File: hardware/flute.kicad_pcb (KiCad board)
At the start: 2 copper layers, 230 x 20 mm, 55 parts, among them J1 Conn_01x02, J3 Conn_01x04, SW1 C, SW2 D, SW3 E, SW4 F, SW5 G, SW6 A, SW7 H, SW8 OCTAVE?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

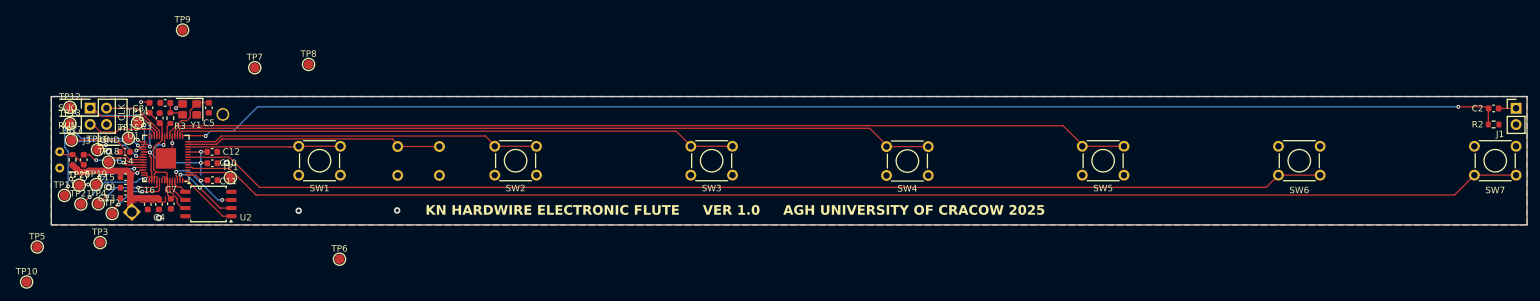
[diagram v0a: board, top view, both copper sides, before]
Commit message: test points placed on the pcb
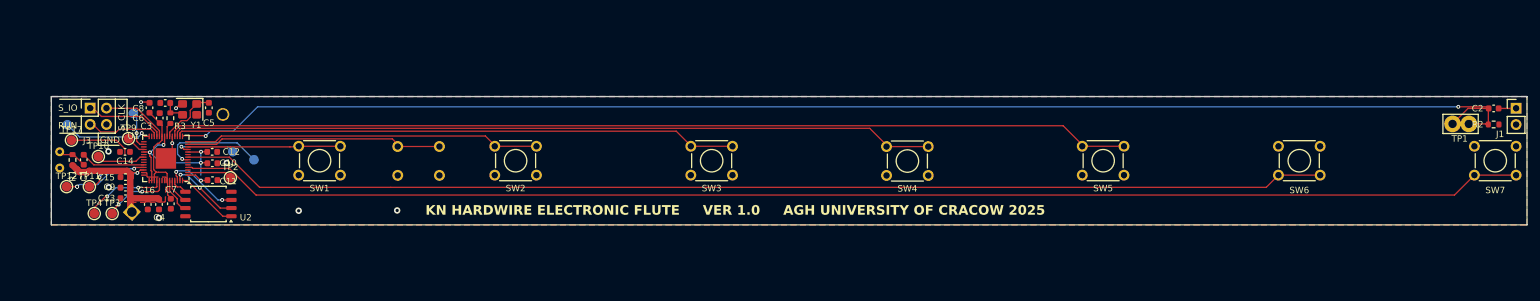
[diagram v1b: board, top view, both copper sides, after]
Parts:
- removed the TP11 at (35.7, 116.8)
- removed TP13, TP15, TP18, TP21: TestPoint, TestPoint:TestPoint_Pad_D1.5mm
- removed the TP3 at (41.3, 124.2)
- removed the TP5 at (31.5, 124.8)
- removed the TP7 at (65.4, 96.9)
- removed the TP9 at (54.2, 91.0)
- added TP1: TestPoint, TestPoint:TestPoint_Bridge_Pitch2.54mm_Drill1.3mm, F.Cu at (252.1, 105.7)
- TP5: renamed from TP6; moved to B.Cu
- TP6: renamed from TP8; moved to B.Cu
- TP7: renamed from TP10; moved to B.Cu
- TP8: renamed from TP12; moved to B.Cu
- moved TP7 25.3 mm to (36.2, 105.8)
- moved TP5 20.4 mm to (65.3, 111.3)
- moved TP6 18.0 mm to (62.0, 110.0)
- moved TP8 9.95 mm to (46.5, 104.0)
- moved TP9 2.87 mm to (45.7, 108.0)
- moved TP12 1.99 mm to (36.1, 115.4)
- moved TP4 1.65 mm to (40.4, 119.6)
- moved TP11 1.12 mm to (39.6, 115.4)
- moved TP10 1.07 mm to (41.0, 110.7)
- renumbered TP16 to TP10, TP19 to TP11, TP20 to TP12, TP1 to TP2, TP2 to TP3, TP14 to TP9
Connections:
- TP2 pad 2: Net-(U1-GPIO0) -> (no net)
- U1 pad 27: Net-(U1-GPIO16) -> /RASPBERRY_PI_PICO/GPIO16
- U1 pad 29: Net-(U1-GPIO18) -> /RASPBERRY_PI_PICO/GPIO18
- U1 pad 31: Net-(U1-GPIO20) -> /RASPBERRY_PI_PICO/GPIO20
- U1 pad 34: Net-(U1-GPIO22) -> /RASPBERRY_PI_PICO/GPIO22
- U1 pad 36: Net-(U1-GPIO24) -> /RASPBERRY_PI_PICO/GPIO24
- U1 pad 37: Net-(U1-GPIO25) -> /RASPBERRY_PI_PICO/GPIO25
- U1 pad 41: Net-(U1-GPIO29_ADC3) -> /RASPBERRY_PI_PICO/GPIO29
- U1 pad 5: Net-(U1-GPIO3) -> /RASPBERRY_PI_PICO/GPIO3
- U1 pad 6: Net-(U1-GPIO4) -> /RASPBERRY_PI_PICO/GPIO4
- U1 pad 9: Net-(U1-GPIO7) -> /RASPBERRY_PI_PICO/GPIO7
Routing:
- net Net-(U1-GPIO18): track 24.0 -> 0.00 mm, vias 2 -> 0
- net Net-(U1-GPIO5): track 0.00 -> 16.5 mm, vias 0 -> 1
- net Net-(U1-GPIO17): track 0.00 -> 14.0 mm, vias 0 -> 1
- net Net-(U1-GPIO20): track 14.0 -> 0.00 mm, vias 2 -> 0
- net Net-(U1-GPIO19): track 18.1 -> 5.86 mm, vias 2 -> 1
- net Net-(U1-GPIO29_ADC3): track 11.7 -> 0.00 mm, vias 2 -> 0
- net /PWM_OUT: track 208.2 -> 217.9 mm
- net Net-(U1-GPIO8): track 0.00 -> 9.50 mm, vias 0 -> 1
- net Net-(U1-GPIO25): track 6.05 -> 0.00 mm
- net Net-(U1-GPIO21): track 7.15 -> 3.09 mm, vias 2 -> 0
- net Net-(U1-GPIO24): track 13.1 -> 9.83 mm
- net Net-(U1-GPIO28_ADC2): track 11.0 -> 13.2 mm, vias 2 -> 3
- net /RASPBERRY_PI_PICO/USB_DM: track 11.2 -> 13.0 mm
- net Net-(U1-GPIO27_ADC1): track 8.89 -> 9.99 mm
- net Net-(U1-GPIO22): track 1.06 -> 0.00 mm
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
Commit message: minor corrections
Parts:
- removed TP1: TestPoint, TestPoint:TestPoint_Bridge_Pitch2.54mm_Drill1.3mm
- removed TP17: TestPoint, TestPoint:TestPoint_Pad_D1.5mm
- added JP1: COUPLING, Jumper:SolderJumper-2_P1.3mm_Open_Pad1.0x1.5mm, F.Cu at (252.7, 105.4)
- added JP2: NO_COUPLING, Jumper:SolderJumper-2_P1.3mm_Open_Pad1.0x1.5mm, F.Cu at (255.5, 105.4)
- moved TP5 0.52 mm to (64.8, 111.1)
- moved TP8 0.28 mm to (46.7, 104.1)
- moved TP6 0.13 mm to (62.0, 110.1)
- moved C15 0.10 mm to (45.2, 114.0)
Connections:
- C2 pad 2: /PWM_OUT -> Net-(JP1-A)
- R2 pad 1: /PWM_OUT -> Net-(JP1-A)
- TP2 pad 2: (no net) -> Net-(U1-GPIO0)
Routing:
- net Net-(U1-GPIO24): track 9.83 -> 0.00 mm
- net Net-(JP1-A): track 0.00 -> 7.74 mm
- net Net-(J1-Pin_1): track 2.74 -> 9.25 mm
- net /PWM_OUT: track 217.9 -> 213.6 mm

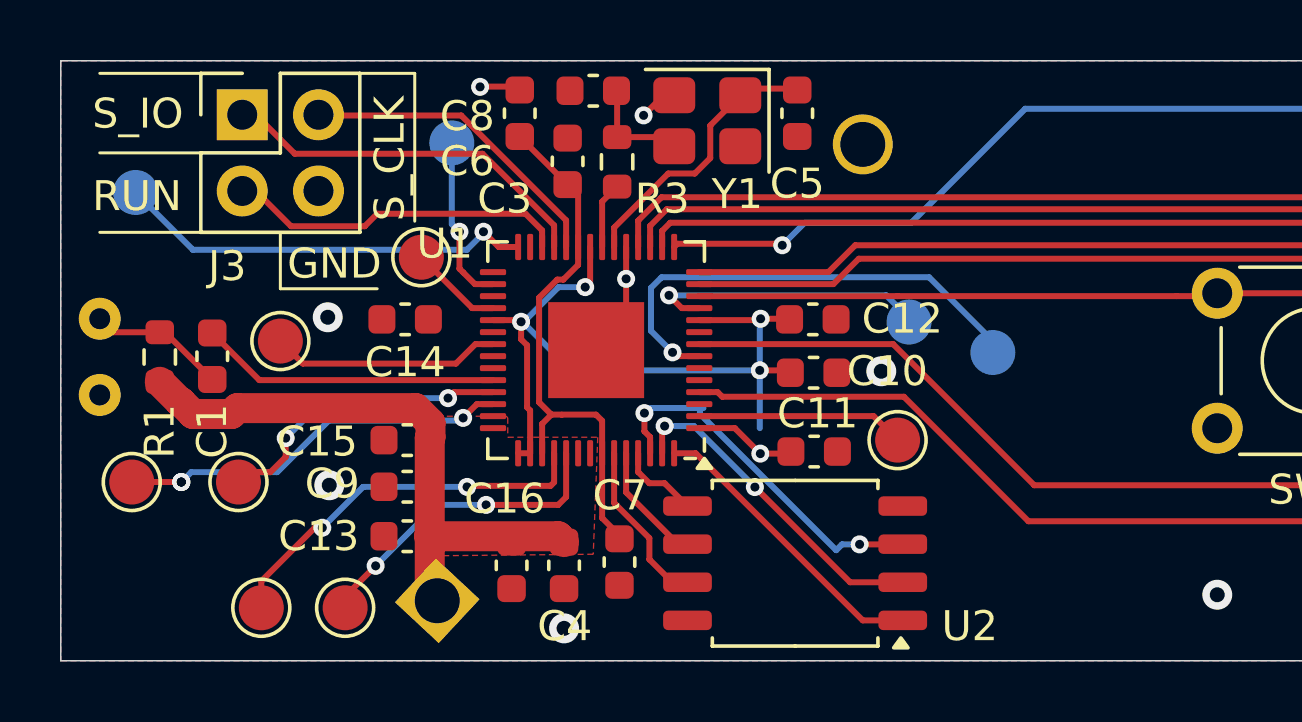
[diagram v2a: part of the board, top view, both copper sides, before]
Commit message: errors with elements placement corrected
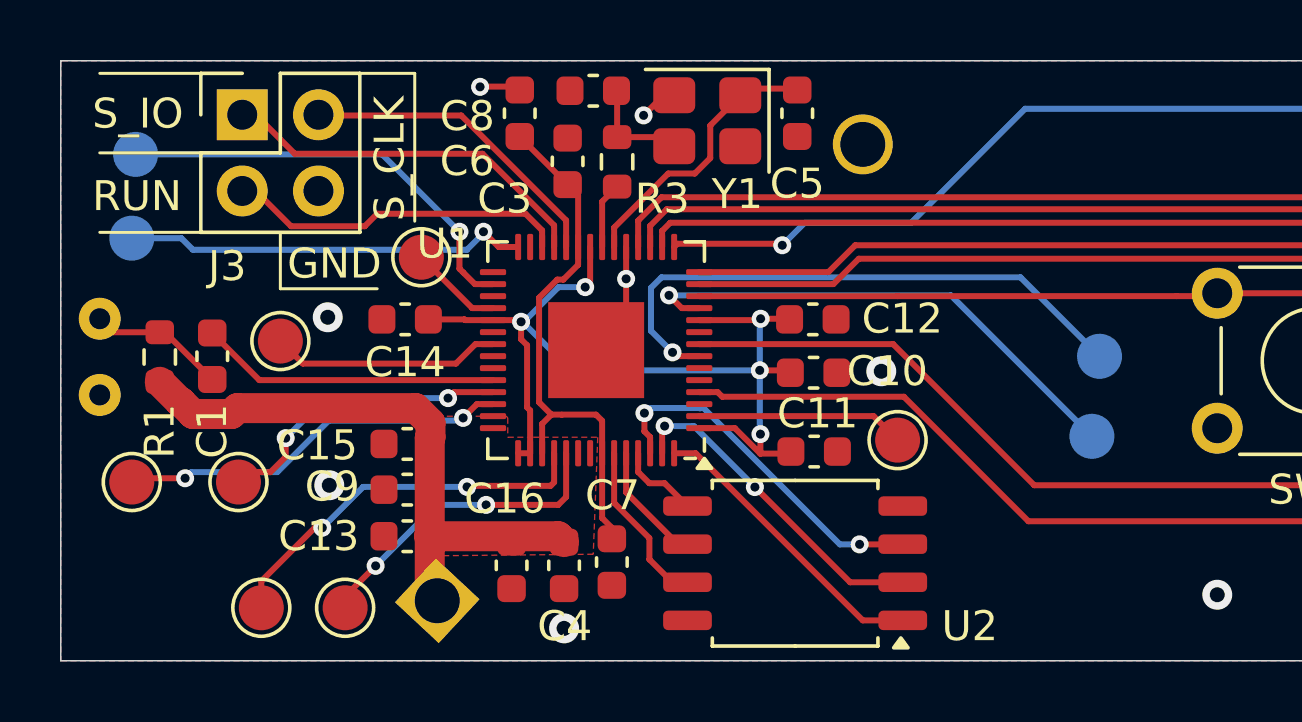
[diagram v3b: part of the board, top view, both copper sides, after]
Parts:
- moved TP8 10.5 mm to (36.2, 104.5)
- moved TP6 7.19 mm to (68.1, 113.9)
- moved TP5 3.56 mm to (68.3, 111.3)
- moved TP7 1.53 mm to (36.1, 107.3)
- moved C7 0.25 mm to (52.1, 118.1)
- moved C15 0.13 mm to (45.2, 114.2)
- moved C9 0.10 mm to (45.2, 115.7)
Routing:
- net Net-(U1-GPIO19): track 5.63 -> 14.4 mm
- net Net-(U1-GPIO8): track 9.63 -> 17.2 mm
- net Net-(U1-GPIO5): track 16.3 -> 19.6 mm
- net +3V3: track 51.0 -> 54.0 mm
- net Net-(U1-GPIO17): track 14.0 -> 13.5 mm
- net Net-(U1-GPIO28_ADC2): track 13.2 -> 13.1 mm, vias 3 -> 2
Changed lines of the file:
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@@
 	(footprint "Capacitor_SMD:C_0603_1608Metric"
 		(layer "F.Cu")
-		(at 45.25 115.6 180)
+		(at 45.25 115.697 180)
 		(descr "Capacitor SMD 0603 (1608 Metric), square (rectangular) end terminal, IPC-7351 nominal, (Body size source: IPC-SM-782 page 76, https://www.pcb-3d.com/wordpress/wp-content/uploads/ipc-sm-782a_amendment_1_and_2.pdf), generated with kicad-footprint-generator")
 		(tags "capacitor")
@@
 	(footprint "Capacitor_SMD:C_0603_1608Metric"
 		(layer "F.Cu")
-		(at 52.324 118.11 -90)
+		(at 52.07 118.11 -90)
 		(descr "Capacitor SMD 0603 (1608 Metric), square (rectangular) end terminal, IPC-7351 nominal, (Body size source: IPC-SM-782 page 76, https://www.pcb-3d.com/wordpress/wp-content/uploads/ipc-sm-782a_amendment_1_and_2.pdf), generated with kicad-footprint-generator")
 		(tags "capacitor")
@@
 	(footprint "Capacitor_SMD:C_0603_1608Metric"
 		(layer "F.Cu")
-		(at 45.25 114.046 180)
+		(at 45.25 114.173 180)
 		(descr "Capacitor SMD 0603 (1608 Metric), square (rectangular) end terminal, IPC-7351 nominal, (Body size source: IPC-SM-782 page 76, https://www.pcb-3d.com/wordpress/wp-content/uploads/ipc-sm-782a_amendment_1_and_2.pdf), generated with kicad-footprint-generator")
 		(tags "capacitor")
@@
 	(footprint "TestPoint:TestPoint_Pad_D1.5mm"
 		(layer "B.Cu")
-		(at 61.976 110.109)
+		(at 68.072 113.919)
 		(descr "SMD pad as test Point, diameter 1.5mm")
 		(tags "test point SMD pad")
@@
 	(footprint "TestPoint:TestPoint_Pad_D1.5mm"
 		(layer "B.Cu")
-		(at 46.736 104.14)
+		(at 36.195 104.521)
 		(descr "SMD pad as test Point, diameter 1.5mm")
 		(tags "test point SMD pad")
@@
 	(footprint "TestPoint:TestPoint_Pad_D1.5mm"
 		(layer "B.Cu")
-		(at 64.77 111.125)
+		(at 68.326 111.252)
 		(descr "SMD pad as test Point, diameter 1.5mm")
 		(tags "test point SMD pad")
@@
 	(footprint "TestPoint:TestPoint_Pad_D1.5mm"
 		(layer "B.Cu")
-		(at 36.195 105.791)
+		(at 36.068 107.315)
 		(descr "SMD pad as test Point, diameter 1.5mm")
 		(tags "test point SMD pad")
@@
 	)
 	(segment
-		(start 52.298 117.195)
-		(end 51.745926 116.642926)
-		(width 0.2)
-		(layer "F.Cu")
-		(net 2)
-	)
-	(segment
 		(start 50.595434 105.528381)
 		(end 50.945926 105.878873)
@@
 	)
 	(segment
+		(start 51.745926 116.642926)
+		(end 52.07 116.967)
+		(width 0.2)
+		(layer "F.Cu")
+		(net 2)
+	)
+	(segment
+		(start 52.07 116.967)
+		(end 52.07 117.335)
+		(width 0.2)
+		(layer "F.Cu")
+		(net 2)
+	)
+	(segment
 		(start 50.053926 113.196245)
 		(end 49.745926 113.504245)
@@
 	)
 	(segment
+		(start 47.156245 110.021245)
+		(end 45.954926 110.021245)
+		(width 0.2)
+		(layer "F.Cu")
+		(net 5)
+	)
+	(segment
 		(start 38.110204 113.176)
 		(end 37.708204 112.774)
@@
 	)
 	(segment
+		(start 47.180745 110.045745)
+		(end 47.156245 110.021245)
+		(width 0.2)
+		(layer "F.Cu")
+		(net 5)
+	)
+	(segment
 		(start 49.345926 114.483245)
 		(end 48.945926 114.483245)
@@
 	)
 	(segment
+		(start 57.023 113.845745)
+		(end 57.023 114.492574)
+		(width 0.2)
+		(layer "F.Cu")
+		(net 5)
+	)
+	(segment
 		(start 46.25 119.4)
 		(end 46.15 119.4)
@@
 	)
 	(segment
+		(start 57.023 114.492574)
+		(end 57.019074 114.4965)
+		(width 0.2)
+		(layer "F.Cu")
+		(net 5)
+	)
+	(segment
 		(start 49.044926 110.101066)
 		(end 48.952243 110.193749)
@@
 	)
 	(segment
-		(start 48.952243 110.193749)
-		(end 48.945926 110.193749)
+		(start 48.108426 110.045745)
+		(end 47.180745 110.045745)
 		(width 0.2)
 		(layer "F.Cu")
@@
 	)
 	(segment
-		(start 48.727926 117.294245)
-		(end 48.945926 117.076245)
+		(start 48.952243 110.193749)
+		(end 48.945926 110.193749)
 		(width 0.2)
 		(layer "F.Cu")
@@
 	)
 	(segment
-		(start 45.954926 110.021245)
-		(end 45.979426 110.045745)
+		(start 48.727926 117.294245)
+		(end 48.945926 117.076245)
 		(width 0.2)
 		(layer "F.Cu")
@@
 	)
 	(via
-		(at 57.019074 114.4965)
+		(at 57.023 113.845745)
 		(size 0.6)
 		(drill 0.3)
@@
 	)
 	(segment
-		(start 49.210998 110.221136)
-		(end 50.710107 111.720245)
+		(start 57 111.720245)
+		(end 57 113.822745)
 		(width 0.2)
 		(layer "B.Cu")
@@
 	)
 	(segment
-		(start 57 111.720245)
-		(end 57 113.646745)
+		(start 49.210998 110.221136)
+		(end 50.710107 111.720245)
 		(width 0.2)
 		(layer "B.Cu")
@@
 	)
 	(segment
+		(start 57 113.822745)
+		(end 57.023 113.845745)
+		(width 0.2)
+		(layer "B.Cu")
+		(net 5)
+	)
+	(segment
 		(start 49.171313 110.221136)
 		(end 49.210998 110.221136)
@@
 	)
 	(segment
-		(start 55.005 113.171)
-		(end 55.005 112.990245)
-		(width 0.2)
-		(layer "B.Cu")
-		(net 18)
-	)
-	(segment
-		(start 59.549 117.715)
-		(end 55.005 113.171)
-		(width 0.2)
-		(layer "B.Cu")
-		(net 18)
-	)
-	(segment
-		(start 59.549 117.715)
-		(end 59.743755 117.520245)
+		(start 60.327926 117.520245)
+		(end 59.670245 117.520245)
 		(width 0.2)
 		(layer "B.Cu")
@@
 	)
 	(segment
-		(start 59.743755 117.520245)
-		(end 60.327926 117.520245)
+		(start 55.126245 112.976245)
+		(end 54.991 112.976245)
 		(width 0.2)
 		(layer "B.Cu")
@@
 	)
 	(segment
-		(start 55.126245 112.976245)
-		(end 54.991 112.976245)
+		(start 59.670245 117.520245)
+		(end 55.126245 112.976245)
 		(width 0.2)
 		(layer "B.Cu")
@@
 	)
 	(segment
-		(start 54.09278 111.120246)
-		(end 53.374 110.401466)
-		(width 0.2)
-		(layer "B.Cu")
-		(net 34)
-	)
-	(segment
-		(start 64.77 110.744)
-		(end 64.77 111.125)
+		(start 65.693 108.619)
+		(end 68.326 111.252)
 		(width 0.2)
 		(layer "B.Cu")
@@
 	)
 	(segment
-		(start 53.374 108.971057)
-		(end 53.726057 108.619)
+		(start 54.09278 111.120246)
+		(end 53.374 110.401466)
 		(width 0.2)
 		(layer "B.Cu")
@@
 	)
 	(segment
-		(start 62.645 108.619)
-		(end 64.77 110.744)
+		(start 53.726057 108.619)
+		(end 65.693 108.619)
 		(width 0.2)
 		(layer "B.Cu")
@@
 	)
 	(segment
-		(start 53.726057 108.619)
-		(end 62.645 108.619)
-		(width 0.2)
-		(layer "B.Cu")
-		(net 34)
-	)
-	(segment
-		(start 65.151 111.125)
-		(end 65.151 111.252)
+		(start 53.374 108.971057)
+		(end 53.726057 108.619)
 		(width 0.2)
 		(layer "B.Cu")
@@
 	)
 	(segment
-		(start 53.975 109.22)
-		(end 61.214 109.22)
-		(width 0.2)
-		(layer "B.Cu")
-		(net 36)
-	)
-	(segment
-		(start 61.976 109.982)
-		(end 61.976 110.109)
+		(start 63.373 109.22)
+		(end 68.072 113.919)
 		(width 0.2)
 		(layer "B.Cu")
@@
 	)
 	(segment
-		(start 61.214 109.22)
-		(end 61.976 109.982)
+		(start 53.975 109.22)
+		(end 63.373 109.22)
 		(width 0.2)
 		(layer "B.Cu")
@@
 	)
 	(segment
+		(start 47.790003 107.14994)
+		(end 47.238943 107.701)
+		(width 0.2)
+		(layer "B.Cu")
+		(net 38)
+	)
+	(segment
 		(start 38.105 107.701)
-		(end 36.195 105.791)
+		(end 37.719 107.315)
 		(width 0.2)
 		(layer "B.Cu")
@@
 	)
 	(segment
-		(start 47.790003 107.14994)
-		(end 47.238943 107.701)
+		(start 37.719 107.315)
+		(end 36.068 107.315)
 		(width 0.2)
 		(layer "B.Cu")
@@
 	)
 	(segment
-		(start 46.736 106.846)
-		(end 46.99 107.1)
+		(start 44.411 104.521)
+		(end 36.195 104.521)
 		(width 0.2)
 		(layer "B.Cu")
@@
 	)
 	(segment
-		(start 46.736 104.14)
-		(end 46.736 106.846)
+		(start 46.99 107.1)
+		(end 44.411 104.521)
 		(width 0.2)
 		(layer "B.Cu")
@@
 	)
 	(segment
-		(start 37.719 115.443)
+		(start 36.195 115.316)
 		(end 36.068 115.443)
 		(width 0.2)
@@
 		(net 47)
 	)
-	(via
-		(at 37.719 115.443)
-		(size 0.6)
-		(drill 0.3)
-		(layers "F.Cu" "B.Cu")
+	(segment
+		(start 37.846 115.316)
+		(end 36.195 115.316)
+		(width 0.2)
+		(layer "F.Cu")
 		(net 47)
 	)
 	(via
-		(at 37.719 115.443)
+		(at 37.846 115.316)
 		(size 0.6)
 		(drill 0.3)
@@
 	(segment
 		(start 38.0492 115.1128)
-		(end 37.719 115.443)
-		(width 0.2)
-		(layer "B.Cu")
-		(net 47)
-	)
-	(segment
-		(start 37.719 115.443)
-		(end 37.592 115.443)
+		(end 37.846 115.316)
 		(width 0.2)
 		(layer "B.Cu")

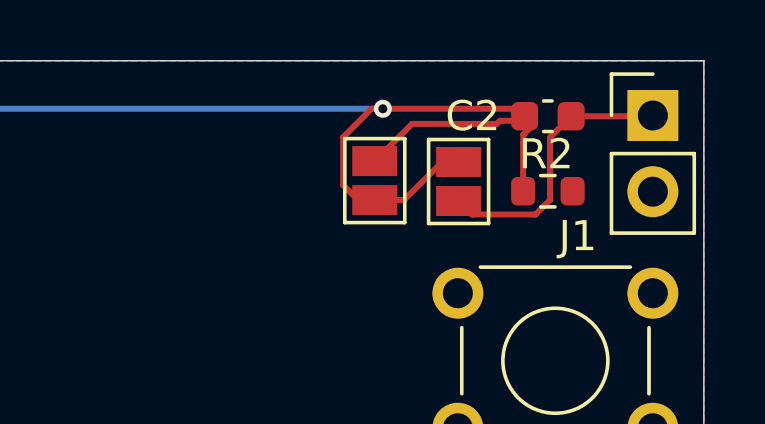
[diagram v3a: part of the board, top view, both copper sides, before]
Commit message: error with PWM_OUT corrected
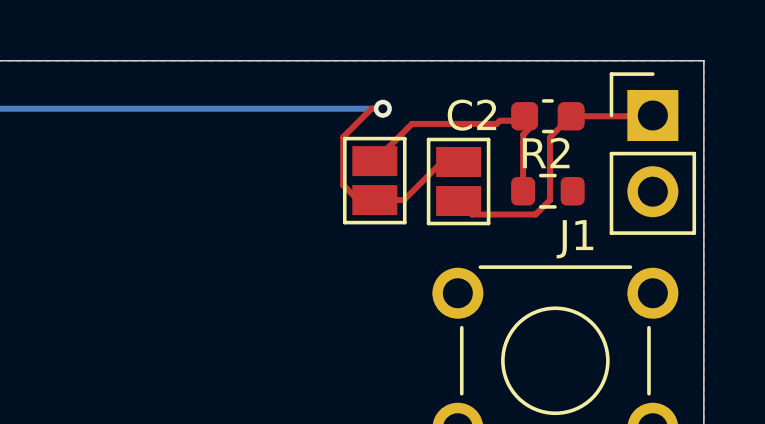
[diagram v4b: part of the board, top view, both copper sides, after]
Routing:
- net /PWM_OUT: track 213.6 -> 208.7 mm
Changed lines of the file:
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@@
-	)
-	(segment
-		(start 257.475 103)
-		(end 257.725 103.25)
-		(width 0.2)
-		(layer "F.Cu")
-		(net 20)
 	)
 	(segment
@@
 	)
 	(segment
-		(start 253 103)
-		(end 257.475 103)
-		(width 0.2)
-		(layer "F.Cu")
-		(net 20)
-	)
-	(segment
 		(start 251.679 103.944)
 		(end 252.623 103)
@@
 		(start 253.702 106.045)
 		(end 254.972 104.775)
-		(width 0.2)
-		(layer "F.Cu")
-		(net 20)
-	)
-	(segment
-		(start 257.675 103.3)
-		(end 257.725 103.25)
 		(width 0.2)
 		(layer "F.Cu")
@@
 	)
 	(segment
+		(start 257.475 103)
+		(end 257.725 103.25)
+		(width 0.2)
+		(layer "F.Cu")
+		(net 50)
+	)
+	(segment
 		(start 256.898 103.401)
 		(end 257.274 103.401)
@@
 		(width 0.2)
 		(layer "F.Cu")
+		(net 50)
+	)
+	(segment
+		(start 257.675 103.3)
+		(end 257.725 103.25)
+		(width 0.2)
+		(layer "F.Cu")

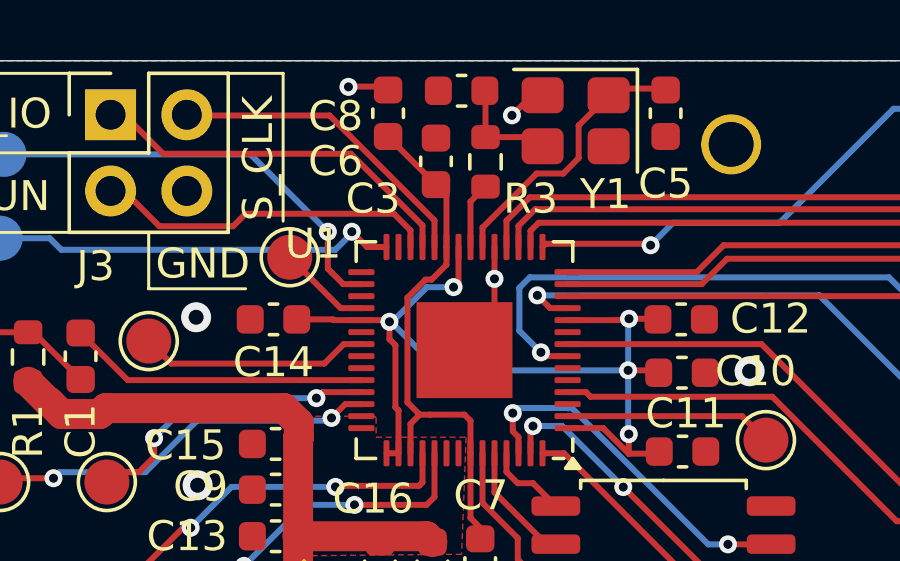
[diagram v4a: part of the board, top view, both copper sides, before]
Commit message: problem with soldermask corrected
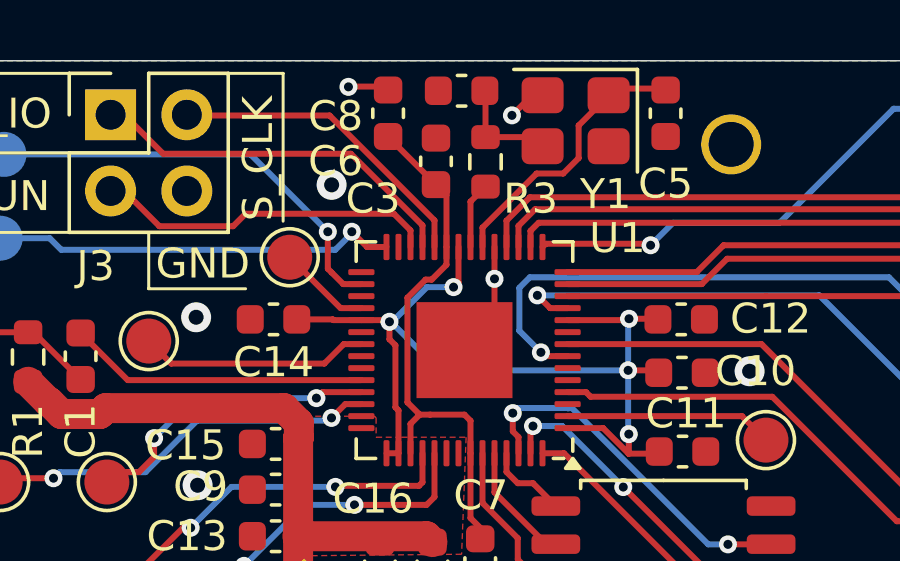
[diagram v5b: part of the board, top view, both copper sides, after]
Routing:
- net GND: track 7.40 -> 7.50 mm, vias 9 -> 10
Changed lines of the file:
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@@
 			(layer "F.CrtYd")
 		)
-		(pad "2" smd circle
+		(pad "1" smd circle
 			(at 0 0)
 			(size 1.5 1.5)
@@
 		(tags "QFN NoLead")
 		(property "Reference" "U1"
-			(at 5.045926 3.545745 0)
+			(at -5.096074 3.730745 0)
 			(layer "F.SilkS")
 			(effects
@@
 	)
 	(segment
+		(start 44.333681 109.95)
+		(end 44.404926 110.021245)
+		(width 0.2)
+		(layer "F.Cu")
+		(net 1)
+	)
+	(segment
 		(start 47.686926 102.261245)
 		(end 47.677926 102.270245)
@@
 		(size 1)
 		(drill 0.5)
+		(layers "F.Cu" "B.Cu")
+		(free yes)
+		(net 1)
+	)
+	(via
+		(at 47.117 105.537)
+		(size 1)
+		(drill 0.5)
